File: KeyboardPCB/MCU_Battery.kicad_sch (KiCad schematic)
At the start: 41 parts, among them Q1 CSD17527Q5A, Q2 CSD17527Q5A, U1 ATmega32U4-M, U2 TPS61236PRWLT, U3 BQ24193RGER, U4 BQ297xy, Y1 ECS-160-7-33B-CKL-TR

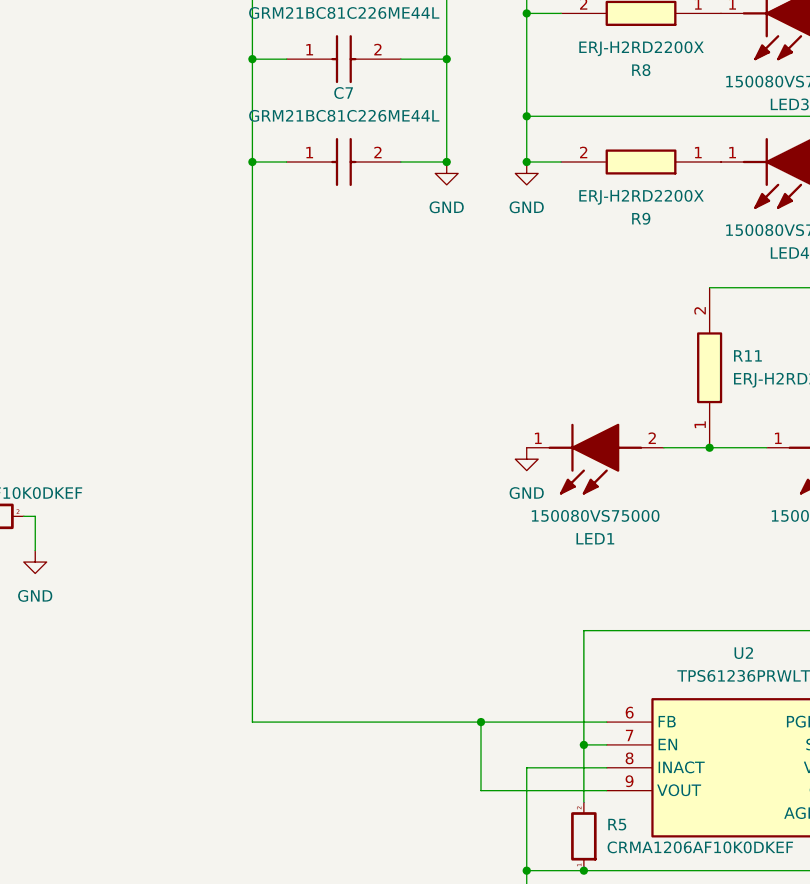
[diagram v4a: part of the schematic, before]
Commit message: Added switch and modified pcb to account for it
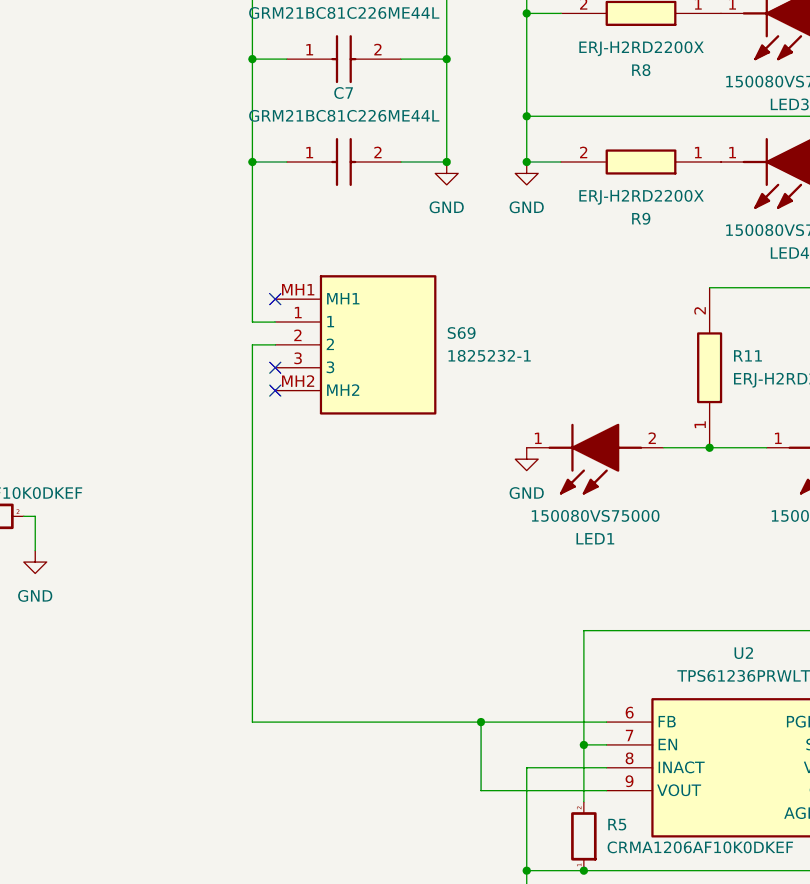
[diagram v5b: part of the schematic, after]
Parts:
- added S69: 1825232-1, keyboard_syms:18252321, symbol keyboard_syms:1825232-1
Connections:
- net VBUSOUT: now also S69.1; no longer U2.6 (FB), U2.9 (VOUT)
- new net: S69.2, U2.6 (FB), U2.9 (VOUT)
- no-connect marks 7 -> 10
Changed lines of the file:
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@@
   (junction (at 40.64 41.91) (diameter 0) (color 0 0 0 0)
   )
+  (junction (at 250.19 20.32) (diameter 0) (color 0 0 0 0)
+  )
+  (junction (at 55.88 36.83) (diameter 0) (color 0 0 0 0)
+  )
+  (junction (at 242.57 45.72) (diameter 0) (color 0 0 0 0)
+  )
+  (junction (at 219.71 15.24) (diameter 0) (color 0 0 0 0)
+  )
+  (junction (at 255.27 152.4) (diameter 0) (color 0 0 0 0)
+  )
+  (junction (at 129.54 39.37) (diameter 0) (color 0 0 0 0)
+  )
+  (junction (at 261.62 118.11) (diameter 0) (color 0 0 0 0)
+  )
+  (junction (at 179.07 157.48) (diameter 0) (color 0 0 0 0)
+  )
+  (junction (at 217.17 138.43) (diameter 0) (color 0 0 0 0)
+  )
+  (junction (at 209.55 157.48) (diameter 0) (color 0 0 0 0)
+  )
+  (junction (at 248.92 139.7) (diameter 0) (color 0 0 0 0)
+  )
+  (junction (at 129.54 27.94) (diameter 0) (color 0 0 0 0)
+  )
+  (junction (at 273.05 45.72) (diameter 0) (color 0 0 0 0)
+  )
+  (junction (at 71.12 120.65) (diameter 0) (color 0 0 0 0)
+  )
+  (junction (at 160.02 34.29) (diameter 0) (color 0 0 0 0)
+  )
+  (junction (at 38.1 54.61) (diameter 0) (color 0 0 0 0)
+  )
+  (junction (at 40.64 46.99) (diameter 0) (color 0 0 0 0)
+  )
+  (junction (at 246.38 73.66) (diameter 0) (color 0 0 0 0)
+  )
+  (junction (at 17.78 54.61) (diameter 0) (color 0 0 0 0)
+  )
+  (junction (at 227.33 157.48) (diameter 0) (color 0 0 0 0)
+  )
+  (junction (at 242.57 58.42) (diameter 0) (color 0 0 0 0)
+  )
+  (junction (at 224.79 91.44) (diameter 0) (color 0 0 0 0)
+  )
   (junction (at 129.54 50.8) (diameter 0) (color 0 0 0 0)
   )
-  (junction (at 250.19 20.32) (diameter 0) (color 0 0 0 0)
-  )
-  (junction (at 55.88 36.83) (diameter 0) (color 0 0 0 0)
-  )
-  (junction (at 242.57 45.72) (diameter 0) (color 0 0 0 0)
-  )
-  (junction (at 219.71 15.24) (diameter 0) (color 0 0 0 0)
-  )
-  (junction (at 255.27 152.4) (diameter 0) (color 0 0 0 0)
-  )
-  (junction (at 129.54 39.37) (diameter 0) (color 0 0 0 0)
-  )
-  (junction (at 261.62 118.11) (diameter 0) (color 0 0 0 0)
-  )
-  (junction (at 179.07 157.48) (diameter 0) (color 0 0 0 0)
-  )
-  (junction (at 217.17 138.43) (diameter 0) (color 0 0 0 0)
-  )
-  (junction (at 209.55 157.48) (diameter 0) (color 0 0 0 0)
-  )
-  (junction (at 248.92 139.7) (diameter 0) (color 0 0 0 0)
-  )
-  (junction (at 129.54 27.94) (diameter 0) (color 0 0 0 0)
-  )
-  (junction (at 273.05 45.72) (diameter 0) (color 0 0 0 0)
-  )
-  (junction (at 71.12 120.65) (diameter 0) (color 0 0 0 0)
-  )
-  (junction (at 160.02 34.29) (diameter 0) (color 0 0 0 0)
-  )
-  (junction (at 38.1 54.61) (diameter 0) (color 0 0 0 0)
-  )
-  (junction (at 40.64 46.99) (diameter 0) (color 0 0 0 0)
-  )
-  (junction (at 246.38 73.66) (diameter 0) (color 0 0 0 0)
-  )
-  (junction (at 17.78 54.61) (diameter 0) (color 0 0 0 0)
-  )
-  (junction (at 227.33 157.48) (diameter 0) (color 0 0 0 0)
-  )
-  (junction (at 242.57 58.42) (diameter 0) (color 0 0 0 0)
-  )
-  (junction (at 224.79 91.44) (diameter 0) (color 0 0 0 0)
-  )
   (junction (at 180.34 82.55) (diameter 0) (color 0 0 0 0)
   )
@@
   (junction (at 166.37 129.54) (diameter 0) (color 0 0 0 0)
   )
+  (no_connect (at 132.08 76.2))
   (no_connect (at 58.42 52.07))
+  (no_connect (at 132.08 66.04))
   (no_connect (at 207.01 55.88))
   (no_connect (at 217.17 73.66))
+  (no_connect (at 132.08 73.66))
   (no_connect (at 207.01 58.42))
   (no_connect (at 38.1 27.94))
@@
     (stroke (width 0) (type default))
   )
+  (wire (pts (xy 129.54 68.58) (xy 129.54 50.8))
+    (stroke (width 0) (type default))
+  )
   (wire (pts (xy 53.34 95.25) (xy 53.34 120.65))
     (stroke (width 0) (type default))
@@
     (stroke (width 0) (type default))
   )
+  (wire (pts (xy 129.54 113.03) (xy 129.54 71.12))
+    (stroke (width 0) (type default))
+  )
   (wire (pts (xy 248.92 58.42) (xy 242.57 58.42))
     (stroke (width 0) (type default))
@@
     (stroke (width 0) (type default))
   )
-  (wire (pts (xy 129.54 50.8) (xy 129.54 113.03))
-    (stroke (width 0) (type default))
-  )
   (wire (pts (xy 203.2 40.64) (xy 203.2 82.55))
     (stroke (width 0) (type default))
@@
     (stroke (width 0) (type default))
   )
+  (wire (pts (xy 129.54 71.12) (xy 132.08 71.12))
+    (stroke (width 0) (type default))
+  )
   (wire (pts (xy 180.34 82.55) (xy 186.69 82.55))
     (stroke (width 0) (type default))
   )
   (wire (pts (xy 241.3 121.92) (xy 203.2 121.92))
+    (stroke (width 0) (type default))
+  )
+  (wire (pts (xy 132.08 68.58) (xy 129.54 68.58))
     (stroke (width 0) (type default))
   )
@@
         )
       )
+    )
+  )
+  (symbol (lib_id "keyboard_syms:1825232-1") (at 143.51 69.85 0) (unit 1)
+    (in_bom yes) (on_board yes) (dnp no) (fields_autoplaced)
+    (property "Reference" "S69" (at 151.13 69.85 0)
+      (effects (font (size 1.27 1.27)) (justify left))
+    )
+    (property "Value" "1825232-1" (at 151.13 72.39 0)
+      (effects (font (size 1.27 1.27)) (justify left))
+    )
+    (property "Footprint" "keyboard_syms:18252321" (at 162.56 164.77 0)
+      (effects (font (size 1.27 1.27)) (justify left top) hide)
+    )
+    (property "Datasheet" "https://componentsearchengine.com/Datasheets/1/1825232-1.pdf" (at 162.56 264.77 0)
+      (effects (font (size 1.27 1.27)) (justify left top) hide)
+    )
+    (property "Height" "3.7" (at 162.56 464.77 0)
+      (effects (font (size 1.27 1.27)) (justify left top) hide)
+    )
+    (property "Manufacturer_Name" "TE Connectivity" (at 162.56 564.77 0)
+      (effects (font (size 1.27 1.27)) (justify left top) hide)
+    )
+    (property "Manufacturer_Part_Number" "1825232-1" (at 162.56 664.77 0)
+      (effects (font (size 1.27 1.27)) (justify left top) hide)
+    )
+    (property "Mouser Part Number" "655-1825232-1" (at 162.56 764.77 0)
+      (effects (font (size 1.27 1.27)) (justify left top) hide)
+    )
+    (property "Mouser Price/Stock" "https://www.mouser.co.uk/ProductDetail/TE-Connectivity-PB/1825232-1?qs=kTKVN3NWb5FosGxaNC1%252BtA%3D%3D" (at 162.56 864.77 0)
+      (effects (font (size 1.27 1.27)) (justify left top) hide)
+    )
+    (property "Arrow Part Number" "1825232-1" (at 162.56 964.77 0)
+      (effects (font (size 1.27 1.27)) (justify left top) hide)
+    )
+    (property "Arrow Price/Stock" "https://www.arrow.com/en/products/1825232-1/te-connectivity?region=europe" (at 162.56 1064.77 0)
+      (effects (font (size 1.27 1.27)) (justify left top) hide)
+    )
+    (pin "1")
+    (pin "2")
+    (pin "3")
+    (pin "MH1")
+    (pin "MH2")
+    (instances
+      (project "KeyboardPCB"
+        (path "/0ddec2b6-b97f-44d3-913e-9f8ffaa22885/0e04ce72-6533-49cc-b4b5-6fa7ba1a6887"
+          (reference "S69") (unit 1)
+        )
+      )
